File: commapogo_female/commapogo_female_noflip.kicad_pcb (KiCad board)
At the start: 4 copper layers, 40.6 x 22.2 mm, 6 parts, among them J1 Conn_02x07_Row_Letter_Last, J2 Conn_02x12_Row_Letter_Last

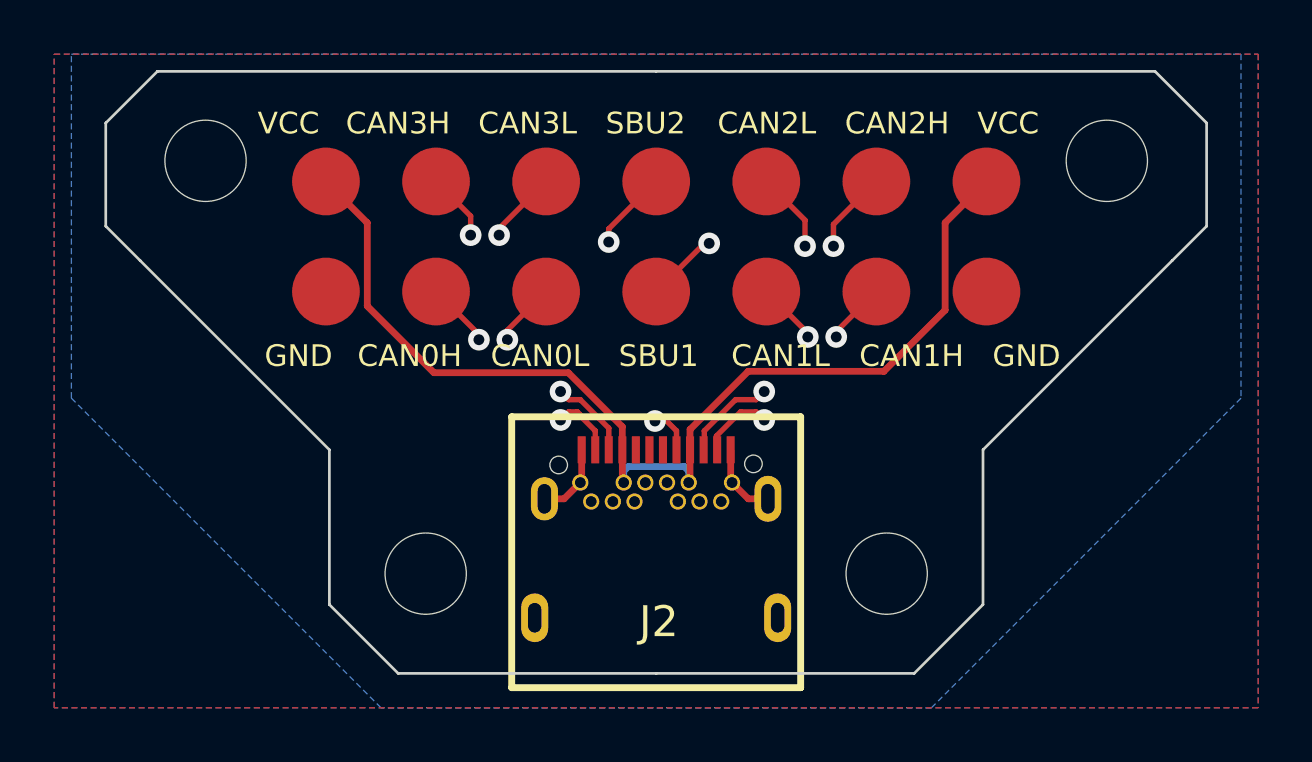
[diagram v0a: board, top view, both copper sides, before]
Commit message: revise pcb with proper calculations
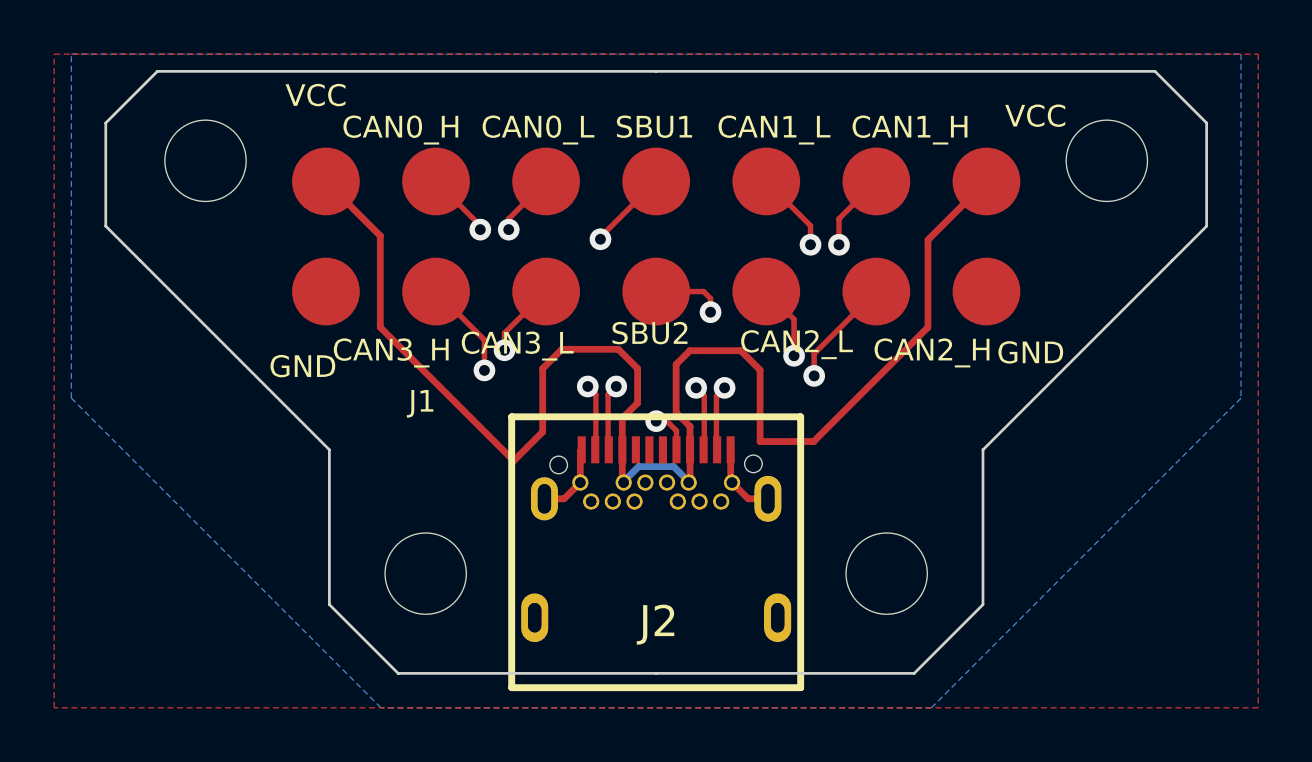
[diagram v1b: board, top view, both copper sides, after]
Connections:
- J1 pad 10: /CAN0_N -> /CAN3_N
- J1 pad 11: /SBU1 -> /SBU2
- J1 pad 12: /CAN1_N -> /CAN2_N
- J1 pad 13: /CAN1_P -> /CAN2_P
- J1 pad 2: /CAN3_P -> /CAN0_P
- J1 pad 3: /CAN3_N -> /CAN0_N
- J1 pad 4: /SBU2 -> /SBU1
- J1 pad 5: /CAN2_N -> /CAN1_N
- J1 pad 6: /CAN2_P -> /CAN1_P
- J1 pad 9: /CAN0_P -> /CAN3_P
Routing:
- net +12V: track 40.6 -> 53.6 mm
- net /CAN2_N: track 14.3 -> 9.62 mm
- net /CAN3_N: track 14.5 -> 10.0 mm
- net /CAN2_P: track 14.3 -> 10.5 mm
- net /CAN3_P: track 14.3 -> 10.5 mm
- net /CAN1_N: track 9.01 -> 12.7 mm
- net /CAN0_P: track 9.27 -> 12.6 mm
- net /CAN0_N: track 9.18 -> 12.5 mm
- net /CAN1_P: track 9.23 -> 12.4 mm
- net /SBU1: track 13.1 -> 12.2 mm
